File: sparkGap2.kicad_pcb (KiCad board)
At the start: 2 copper layers, 55.5 x 60.1 mm, 43 parts, among them J1 9V, J2 IN, J3 OUT, Q1 BS170, SW2 pp, U1 TL072

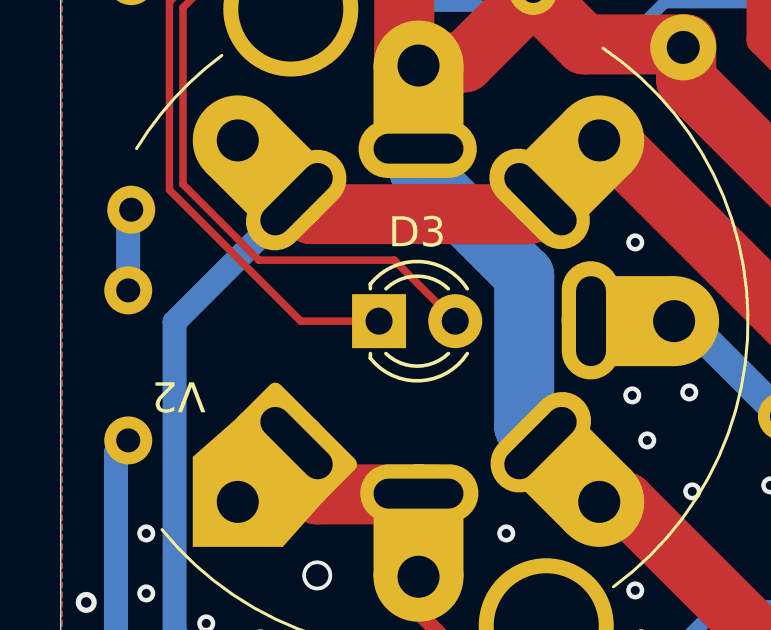
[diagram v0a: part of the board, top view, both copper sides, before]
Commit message: Add missing current limit resistor
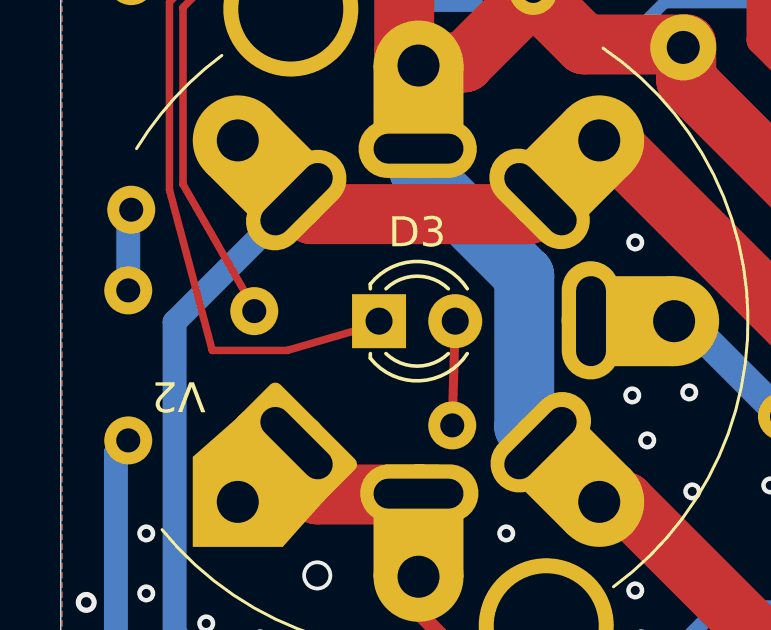
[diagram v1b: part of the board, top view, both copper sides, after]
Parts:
- added R14: 1k, Resistor_THT:R_Axial_DIN0207_L6.3mm_D2.5mm_P7.62mm_Horizontal, B.Cu at (85.3, 102.1)
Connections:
- D3 pad 2: A -> Net-(D3-A)
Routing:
- net A: track 82.2 -> 76.0 mm
- net Net-(D3-A): track 0.00 -> 3.50 mm
- net Net-(D3-K): track 98.6 -> 101.1 mm
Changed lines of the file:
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@@
 	(net 29 "Net-(J2-Pad1N)")
 	(net 30 "Net-(J3-Pad2)")
+	(net 31 "Net-(D3-A)")
 	(footprint "SamacSys_Parts:potentiometer_vert_no_switch"
 		(layer "F.Cu")
@@
 			(layers "*.Cu" "*.Mask")
 			(remove_unused_layers no)
-			(net 2 "A")
+			(net 31 "Net-(D3-A)")
 			(pinfunction "A")
 			(pintype "passive")
@@
 			)
 		)
-		(property "Datasheet" ""
+		(property "Datasheet" "http://www.vishay.com/docs/88503/1n4001.pdf"
 			(at 0 0 90)
 			(layer "B.Fab")
@@
 			)
 		)
-		(property "Description" ""
+		(property "Description" "50V 1A General Purpose Rectifier Diode, DO-41"
 			(at 0 0 90)
 			(layer "B.Fab")
@@
 		)
 	)
+	(footprint "Resistor_THT:R_Axial_DIN0207_L6.3mm_D2.5mm_P7.62mm_Horizontal"
+		(layer "B.Cu")
+		(at 85.3 102.1 150)
+		(descr "Resistor, Axial_DIN0207 series, Axial, Horizontal, pin pitch=7.62mm, 0.25W = 1/4W, length*diameter=6.3*2.5mm^2, http://cdn-reichelt.de/documents/datenblatt/B400/1_4W%23YAG.pdf")
+		(tags "Resistor Axial_DIN0207 series Axial Horizontal pin pitch 7.62mm 0.25W = 1/4W length 6.3mm diameter 2.5mm")
+		(property "Reference" "R14"
+			(at 3.849877 0.17292 150)
+			(layer "B.SilkS")
+			(effects
+				(font
+					(size 1 1)
+					(thickness 0.15)
+				)
+				(justify mirror)
+			)
+		)
+		(property "Value" "1k"
+			(at 3.81 -2.37 150)
+			(layer "B.Fab")
+			(effects
+				(font
+					(size 1 1)
+					(thickness 0.15)
+				)
+				(justify mirror)
+			)
+		)
+		(property "Datasheet" "~"
+			(at 0 0 150)
+			(layer "B.Fab")
+			(hide yes)
+			(effects
+				(font
+					(size 1.27 1.27)
+					(thickness 0.15)
+				)
+				(justify mirror)
+			)
+		)
+		(property "Description" "Resistor, small symbol"
+			(at 0 0 150)
+			(layer "B.Fab")
+			(hide yes)
+			(effects
+				(font
+					(size 1.27 1.27)
+					(thickness 0.15)
+				)
+				(justify mirror)
+			)
+		)
+		(property ki_fp_filters "R_*")
+		(sheetname "/")
+		(sheetfile "sparkGap2.kicad_sch")
+		(attr through_hole)
+		(fp_line
+			(start 7.080002 -1.370001)
+			(end 7.08 -1.04)
+			(stroke
+				(width 0.12)
+				(type solid)
+			)
+			(layer "B.SilkS")
+		)
+		(fp_line
+			(start 7.08 1.369999)
+			(end 7.08 1.040001)
+			(stroke
+				(width 0.12)
+				(type solid)
+			)
+			(layer "B.SilkS")
+		)
+		(fp_line
+			(start 0.540001 -1.370002)
+			(end 7.080002 -1.370001)
+			(stroke
+				(width 0.12)
+				(type solid)
+			)
+			(layer "B.SilkS")
+		)
+		(fp_line
+			(start 0.54 -1.039999)
+			(end 0.540001 -1.370002)
+			(stroke
+				(width 0.12)
+				(type solid)
+			)
+			(layer "B.SilkS")
+		)
+		(fp_line
+			(start 0.540001 1.039999)
+			(end 0.539998 1.369999)
+			(stroke
+				(width 0.12)
+				(type solid)
+			)
+			(layer "B.SilkS")
+		)
+		(fp_line
+			(start 0.539998 1.369999)
+			(end 7.08 1.369999)
+			(stroke
+				(width 0.12)
+				(type solid)
+			)
+			(layer "B.SilkS")
+		)
+		(fp_poly
+			(pts
+				(xy -1.049999 1.499999) (xy -1.050001 -1.500001) (xy 8.670001 -1.5) (xy 8.670002 1.500001)
+			)
+			(stroke
+				(width 0.05)
+				(type solid)
+			)
+			(fill no)
+			(layer "B.CrtYd")
+		)
+		(fp_line
+			(start 7.620001 0.000002)
+			(end 6.960001 -0.000001)
+			(stroke
+				(width 0.1)
+				(type solid)
+			)
+			(layer "B.Fab")
+		)
+		(fp_line
+			(start 0 0)
+			(end 0.659998 0.000001)
+			(stroke
+				(width 0.1)
+				(type solid)
+			)
+			(layer "B.Fab")
+		)
+		(fp_poly
+			(pts
+				(xy 0.66 1.25) (xy 0.659999 -1.25) (xy 6.960001 -1.249999) (xy 6.960003 1.25)
+			)
+			(stroke
+				(width 0.1)
+				(type solid)
+			)
+			(fill no)
+			(layer "B.Fab")
+		)
+		(fp_text user "${REFERENCE}"
+			(at 3.81 -0.000001 150)
+			(layer "B.Fab")
+			(effects
+				(font
+					(size 1 1)
+					(thickness 0.15)
+				)
+				(justify mirror)
+			)
+		)
+		(pad "1" thru_hole circle
+			(at 0 0 150)
+			(size 1.6 1.6)
+			(drill 0.8)
+			(layers "*.Cu" "*.Mask")
+			(remove_unused_layers no)
+			(net 31 "Net-(D3-A)")
+			(pintype "passive")
+		)
+		(pad "2" thru_hole circle
+			(at 7.620001 0.000002 150)
+			(size 1.6 1.6)
+			(drill 0.8)
+			(layers "*.Cu" "*.Mask")
+			(remove_unused_layers no)
+			(net 2 "A")
+			(pintype "passive")
+		)
+		(embedded_fonts no)
+		(model "${KICAD9_3DMODEL_DIR}/Resistor_THT.3dshapes/R_Axial_DIN0207_L6.3mm_D2.5mm_P7.62mm_Horizontal.step"
+			(offset
+				(xyz 0 0 0)
+			)
+			(scale
+				(xyz 1 1 1)
+			)
+			(rotate
+				(xyz 0 0 0)
+			)
+		)
+	)
 	(footprint "Package_TO_SOT_THT:TO-92_Inline"
 		(layer "B.Cu")
@@
 			)
 		)
-		(property "Datasheet" ""
+		(property "Datasheet" "~"
 			(at 0 0 90)
 			(layer "B.Fab")
@@
 			)
 		)
-		(property "Description" ""
+		(property "Description" "Audio Jack, 2 Poles (Mono/TS), Switched Poles (Normalling)"
 			(at 0 0 90)
 			(layer "B.Fab")
@@
 			)
 		)
-		(property "Datasheet" ""
+		(property "Datasheet" "https://assets.nexperia.com/documents/data-sheet/1N4148_1N4448.pdf"
 			(at 0 0 90)
 			(layer "B.Fab")
@@
 			)
 		)
-		(property "Description" ""
+		(property "Description" "100V 0.15A standard switching diode, DO-35"
 			(at 0 0 90)
 			(layer "B.Fab")
@@
 			)
 		)
-		(property "Datasheet" ""
+		(property "Datasheet" "~"
 			(at 0 0 90)
 			(layer "B.Fab")
@@
 			)
 		)
-		(property "Description" ""
+		(property "Description" "Audio Jack, 2 Poles (Mono/TS), Switched Poles (Normalling)"
 			(at 0 0 90)
 			(layer "B.Fab")
@@
 	)
 	(segment
-		(start 83.366473 96.591022)
-		(end 78.851952 96.591022)
-		(width 0.25)
-		(layer "F.Cu")
-		(net 2)
-	)
-	(segment
 		(start 121.432621 98.223985)
 		(end 121.432621 98.6)
@@
 	)
 	(segment
-		(start 120.175428 96.966792)
-		(end 121.432621 98.223985)
-		(width 1)
-		(layer "F.Cu")
-		(net 2)
-	)
-	(segment
-		(start 78.851952 96.591022)
-		(end 76.324901 94.063971)
+		(start 76.324901 94.063971)
+		(end 78.7 98.2)
 		(width 0.25)
 		(layer "F.Cu")
@@
 	)
 	(segment
-		(start 85.4 98.624549)
-		(end 83.366473 96.591022)
-		(width 0.25)
+		(start 120.175428 96.966792)
+		(end 121.432621 98.223985)
+		(width 1)
 		(layer "F.Cu")
 		(net 2)
@@
 	)
 	(segment
-		(start 107.199048 98.581302)
-		(end 107.317746 98.7)
+		(start 79.8 99.6)
+		(end 82.9 98.7)
 		(width 0.25)
 		(layer "F.Cu")
@@
 	)
 	(segment
-		(start 110.537371 84.970389)
-		(end 110.649024 84.970389)
+		(start 107.199048 98.581302)
+		(end 107.317746 98.7)
 		(width 0.25)
 		(layer "F.Cu")
@@
 	)
 	(segment
-		(start 80.247669 98.624549)
-		(end 75.873901 94.250781)
+		(start 110.537371 84.970389)
+		(end 110.649024 84.970389)
 		(width 0.25)
 		(layer "F.Cu")
@@
 	)
 	(segment
+		(start 75.873901 94.250781)
+		(end 77.3 99.6)
+		(width 0.25)
+		(layer "F.Cu")
+		(net 8)
+	)
+	(segment
 		(start 108.481095 87.026665)
 		(end 110.537371 84.970389)
@@
 	)
 	(segment
-		(start 82.86 98.624549)
-		(end 80.247669 98.624549)
+		(start 77.3 99.6)
+		(end 79.8 99.6)
 		(width 0.25)
 		(layer "F.Cu")
@@
 		(net 30)
 	)
+	(segment
+		(start 85.3 102.1)
+		(end 85.4 98.6)
+		(width 0.3)
+		(layer "F.Cu")
+		(net 31)
+	)
 	(zone

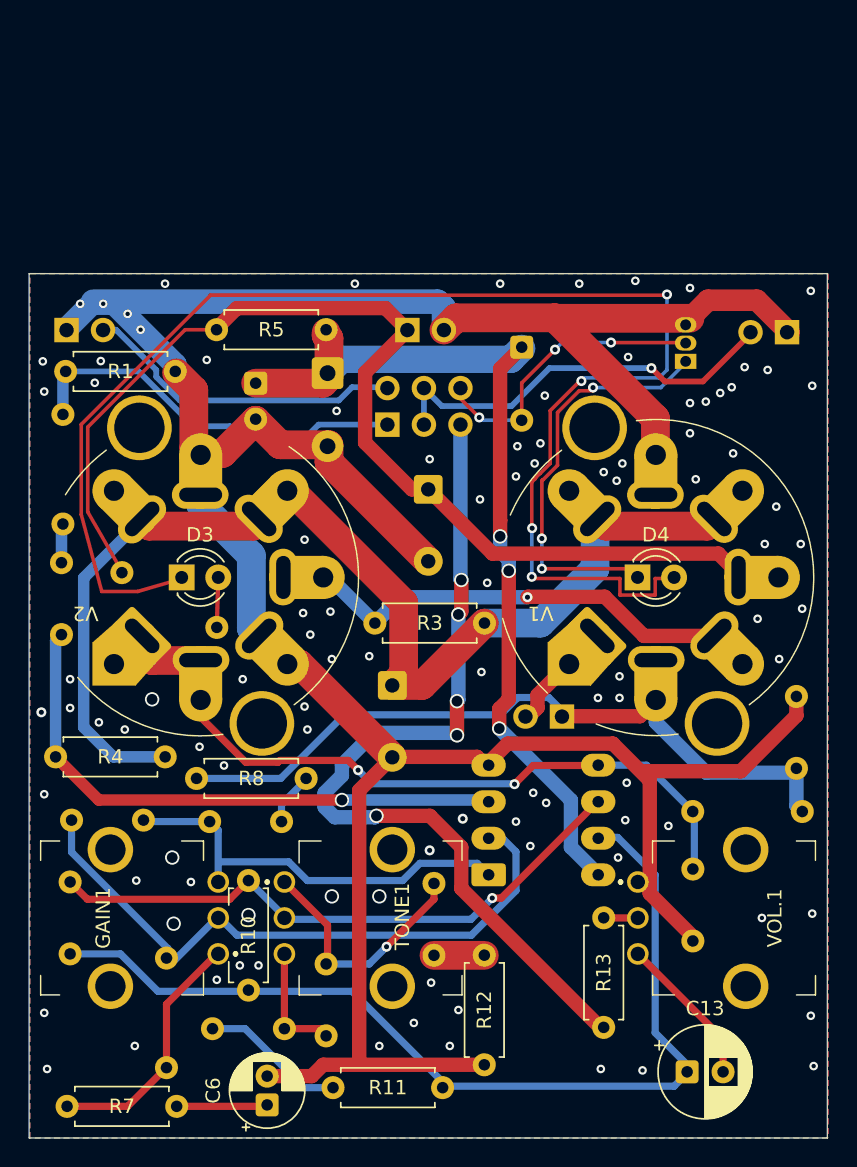
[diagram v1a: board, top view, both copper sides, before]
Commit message: Improve gnd routing and gfx
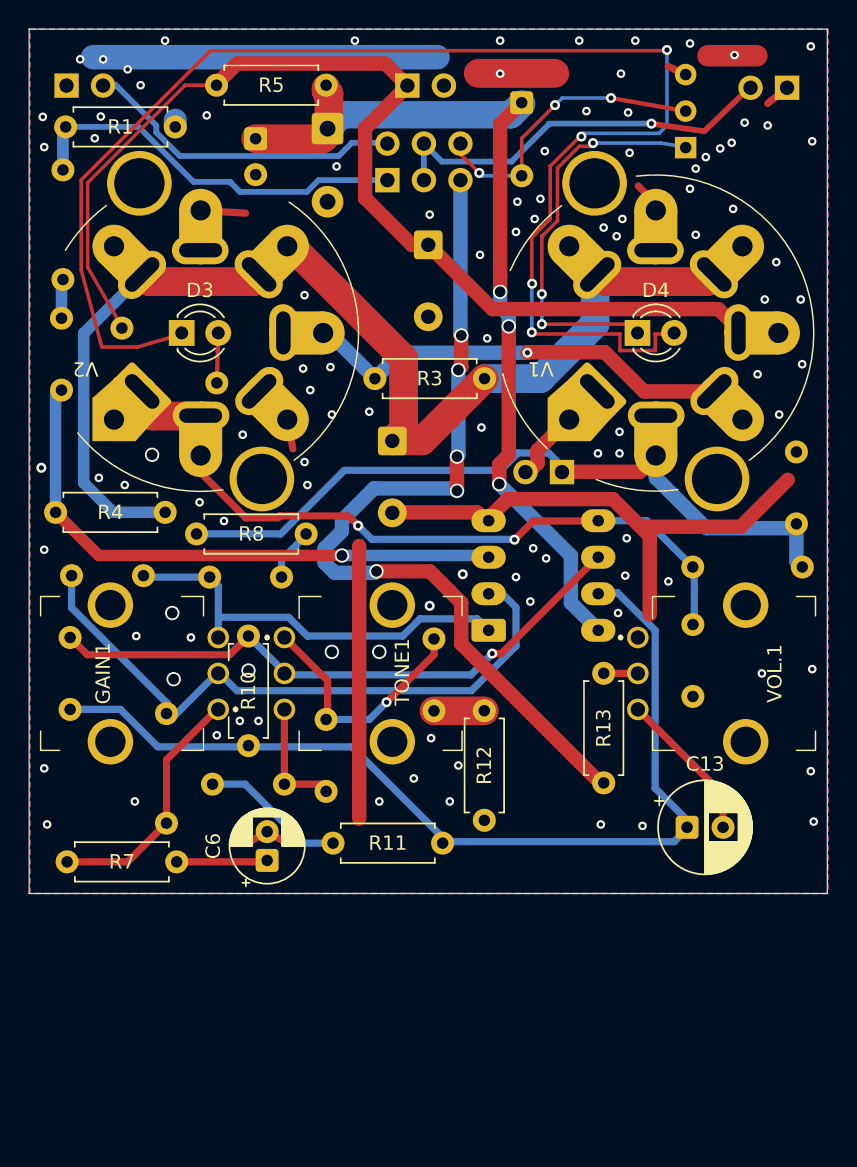
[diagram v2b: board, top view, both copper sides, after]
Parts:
- Q1: footprint Package_TO_SOT_THT:TO-92_Inline -> Package_TO_SOT_THT:TO-92_Inline_Wide
- moved C6 17.0 mm to (88.8, 118.3)
- moved R6 17.0 mm to (81.8, 115.7)
- moved C1 17.0 mm to (100.0, 75.5)
- moved C10 17.0 mm to (75.1, 107.8)
- moved C11 17.0 mm to (85.0, 113.0)
- moved C12 17.0 mm to (100.4, 102.9)
- moved C13 17.0 mm to (118.0, 116.0)
- moved C14 17.0 mm to (92.9, 113.5)
- moved C2 17.0 mm to (74.5, 85.6)
- moved C3 17.0 mm to (97.5, 89.1)
- moved C4 17.0 mm to (88.0, 68.1)
- moved C5 17.0 mm to (80.2, 98.5)
- moved C7 17.0 mm to (84.8, 98.6)
- moved C8 17.0 mm to (125.6, 94.9)
- moved C9 17.0 mm to (118.4, 101.9)
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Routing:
- net Earth: track 208.0 -> 103.3 mm, vias 100 -> 104
- net Net-(D4-K): track 28.8 -> 28.0 mm
- net Net-(J3-Pad2): track 28.9 -> 28.3 mm
- net (no net): vias 1 -> 0
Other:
- board text added: "Clone by Metonic Eng."
- board text added: "ValveWizard"
- board text added: "v0.9.1 2026"

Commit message: correct version info
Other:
- board text added: "v0.2 2026"
- board text removed: "v0.9.1 2026"

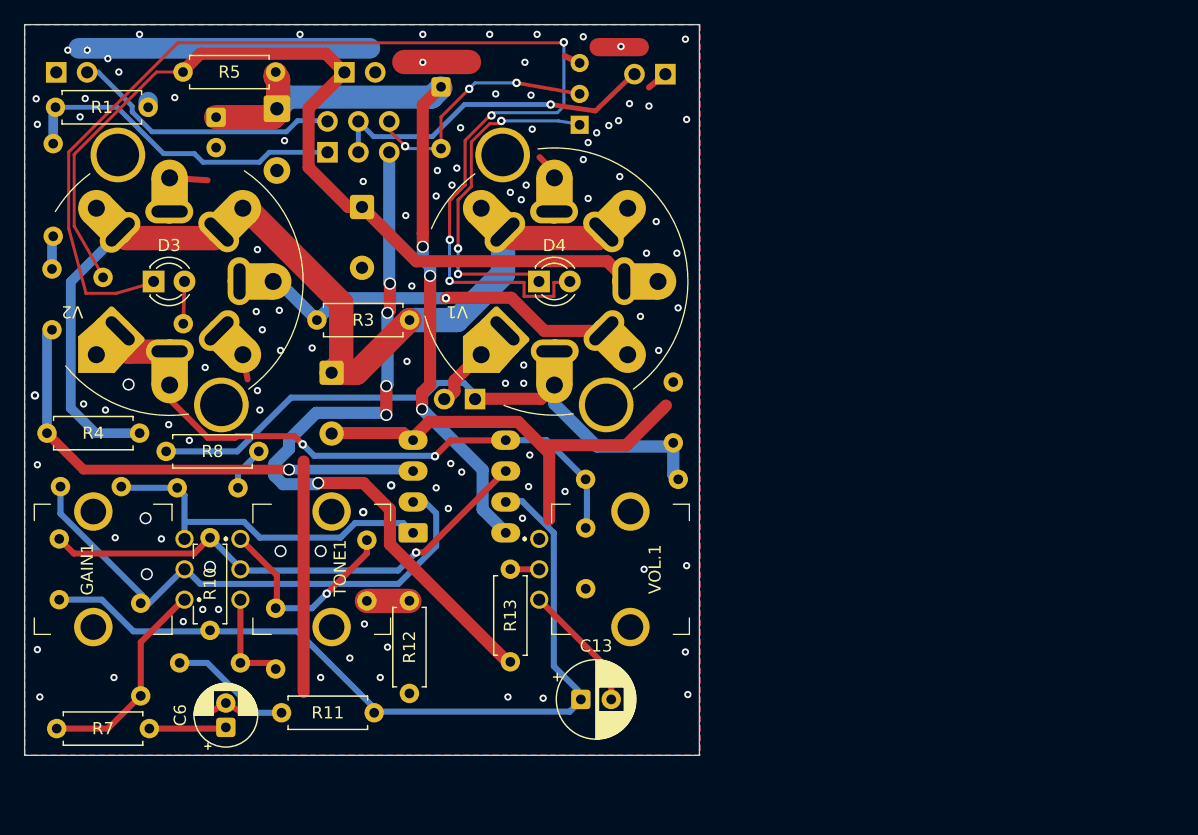
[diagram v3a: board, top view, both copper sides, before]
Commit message: Fix schematic errors. Renumber to match ValveWizard schematic. Improve layout. Switch to 4 layer
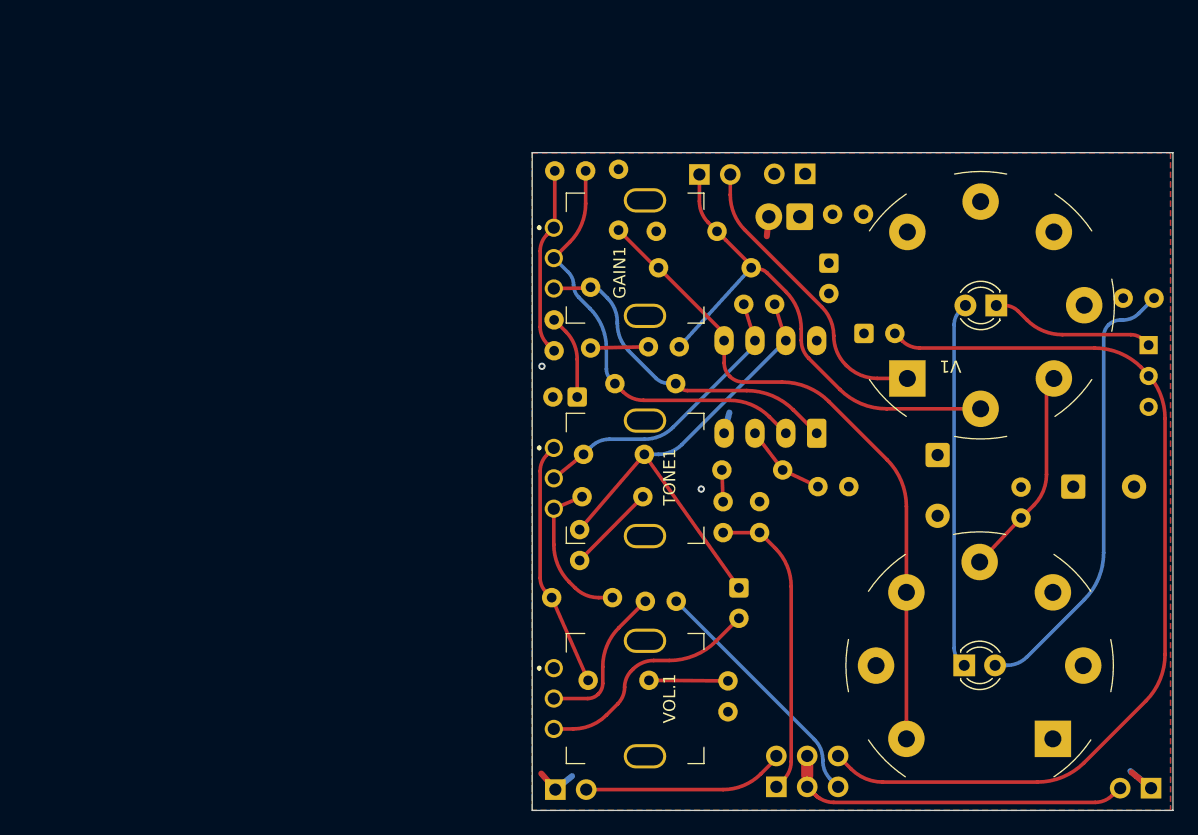
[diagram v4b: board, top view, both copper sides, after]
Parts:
- added REF**: enclosure_1590B_w_jacks_power_switch_B, SamacSys_Parts:enclosure_1590B_w_jacks_power_switch_B, F.Cu at (140.3, 108.2)
- C13, C6: moved to B.Cu
- D1: footprint Diode_THT:D_DO-41_SOD81_P5.08mm_Vertical_AnodeUp -> Diode_THT:D_DO-41_SOD81_P2.54mm_Vertical_AnodeUp
- D2: footprint Diode_THT:D_DO-35_SOD27_P5.08mm_Vertical_AnodeUp -> Diode_THT:D_DO-35_SOD27_P2.54mm_Vertical_AnodeUp
- R1, R10, R11, R12, R13, R3, R4, R5, R7, R8: footprint Resistor_THT:R_Axial_DIN0207_L6.3mm_D2.5mm_P7.62mm_Horizontal -> Resistor_THT:R_Axial_DIN0207_L6.3mm_D2.5mm_P2.54mm_Vertical; moved to B.Cu
- R14, R2, R6: footprint Resistor_THT:R_Axial_DIN0207_L6.3mm_D2.5mm_P7.62mm_Horizontal -> Resistor_THT:R_Axial_DIN0207_L6.3mm_D2.5mm_P2.54mm_Vertical
- R9: value 4.7k -> 47k
- V1, V2: footprint Valves_complete:B7G (7 Pin Mini) Dual Use -> Valves_complete:B7G (7 Pin Mini)-B9A-shield-mount
- moved R14 79.9 mm to (165.1, 83.0), turned to 180 degrees
- moved D3 73.8 mm to (149.5, 113.2)
- moved V2 73.7 mm to (150.8, 113.2), turned to -90 degrees
- moved J2 71.9 mm to (115.9, 123.4)
- moved J3 71.0 mm to (164.9, 123.3)
- moved R1 67.7 mm to (132.7, 102.3), turned to 90 degrees
- moved SW1 63.9 mm to (134.1, 123.2)
- moved R2 63.7 mm to (129.7, 102.3), turned to 90 degrees
- moved R4 63.6 mm to (137.5, 98.5)
- moved C3 61.7 mm to (158.5, 98.5), turned to 0 degrees
- moved C2 61.2 mm to (134.6, 97.1), turned to 180 degrees
- moved R3 60.2 mm to (154.2, 101.1), turned to 90 degrees
- moved R5 57.2 mm to (141.2, 76.1), turned to 180 degrees
- moved R6 55.0 mm to (115.9, 72.5), turned to 0 degrees
- moved C4 51.8 mm to (138.4, 80.1)
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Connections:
- V2 pad 1: Net-(U1B-+) -> 4.5V
- V2 pad 2: Net-(U1B-+) -> 4.5V
- V2 pad 5: 4.5V -> Net-(U1B-+)
- V2 pad 7: 4.5V -> Net-(U1B-+)
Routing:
- net Earth: track 103.3 -> 14.7 mm, vias 104 -> 2
- net Net-(D3-K): track 101.1 -> 30.2 mm, vias 4 -> 0
- net Net-(D2-A): track 20.9 -> 78.0 mm, vias 3 -> 0
- net 9V: track 63.6 -> 17.3 mm, vias 3 -> 0
- net Net-(R13-Pad1): track 61.8 -> 20.6 mm, vias 5 -> 0
- net Net-(D3-A): track 3.50 -> 37.1 mm
- net Net-(U1A-+): track 40.2 -> 6.99 mm, vias 1 -> 0
- net Net-(C10-Pad1): track 67.2 -> 40.1 mm
- net Net-(SW2-B): track 5.68 -> 24.4 mm
- net Net-(U1B--): track 42.6 -> 24.2 mm, vias 1 -> 0
- net Net-(D4-K): track 28.0 -> 13.5 mm, vias 3 -> 0
- net Net-(R3-Pad1): track 30.4 -> 18.1 mm, vias 1 -> 0
- net Net-(R13-Pad2): track 2.52 -> 12.7 mm
- net Net-(U1A--): track 44.7 -> 35.4 mm
- net Net-(C13-Pad2): track 10.8 -> 19.2 mm
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- added copper zone on In1.Cu, net Earth
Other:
- board size 55.5 x 60.1 mm -> 52.7 x 54.1 mm
- copper layers 2 -> 4
- board text added: "Clip SW"
- board text added: "Clone by Metonic"
- board text added: "Foot SW"
- board text added: "IN"
- board text added: "OUT"
- board text removed: "1/4{dblquote} IN"
- board text removed: "1/4{dblquote} OUT"
- board text removed: "1590B Stombox 112x61x31mm"
- board text removed: "Clone by Metonic Eng."
- board text removed: "DPDT"
- board text removed: "SPDT"
